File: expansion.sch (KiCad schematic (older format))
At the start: 3 parts, among them CN1 Expansion bus

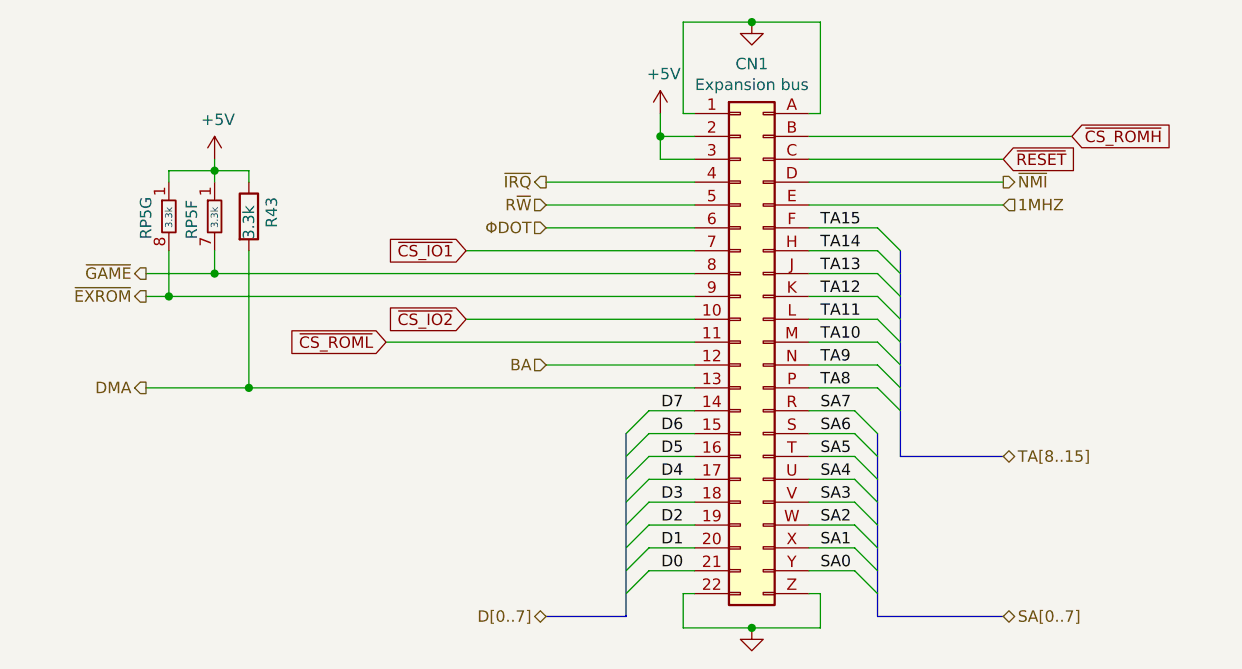
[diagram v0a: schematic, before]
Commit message: Clean up schematic
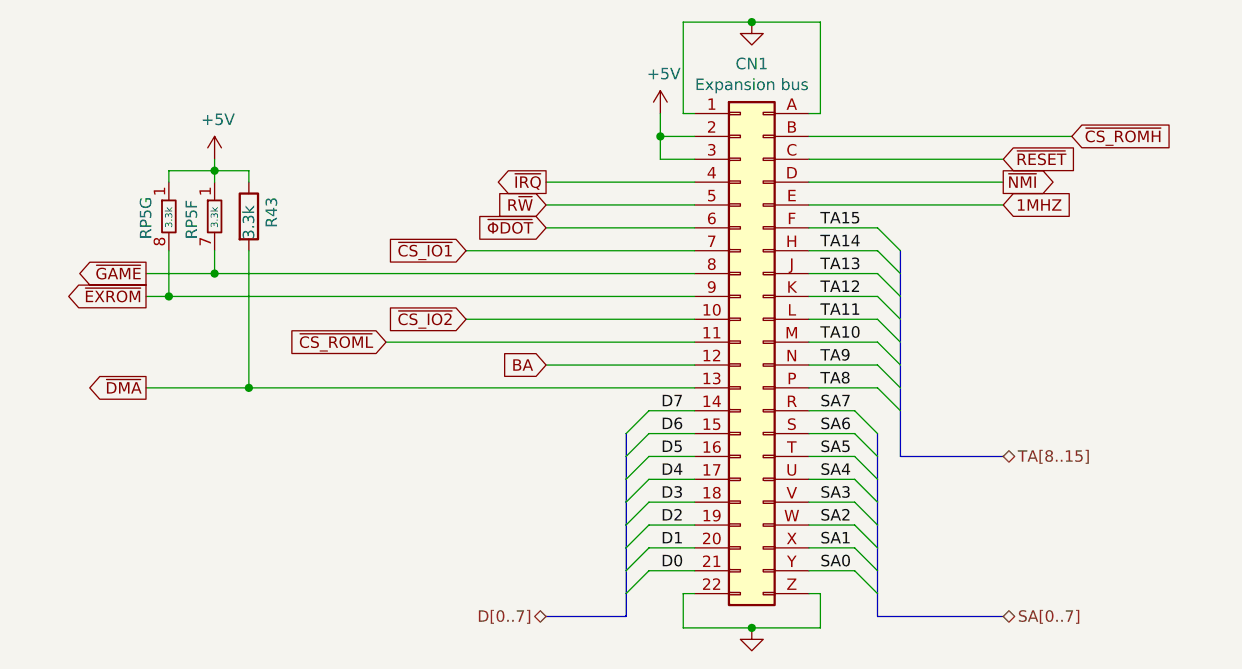
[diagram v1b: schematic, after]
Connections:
- net DMA renamed ~DMA
- net ΦDOT renamed ~ΦDOT
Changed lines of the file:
@@
 	4500 2600 4650 2600
 Connection ~ 4500 2500
-Text HLabel 4000 2700 0    50   Output ~ 0
-~IRQ
-Text HLabel 4000 2800 0    50   Input ~ 0
-R~W
-Text HLabel 4000 2900 0    50   Input ~ 0
-ΦDOT
-Text HLabel 2250 3100 0    50   Output ~ 0
-~GAME
-Text HLabel 2250 3200 0    50   Output ~ 0
-~EXROM
-Text HLabel 4000 3500 0    50   Input ~ 0
-BA
-Text HLabel 2250 3600 0    50   Output ~ 0
-DMA
 Wire Wire Line
 	4650 3700 4450 3700
@@
 Wire Wire Line
 	4000 2700 4650 2700
-Text HLabel 6000 2700 2    50   Output ~ 0
-~NMI
-Text HLabel 6000 2800 2    50   Input ~ 0
-1MHZ
 Wire Wire Line
 	5150 2800 6000 2800
@@
 Wire Bus Line
 	5550 3000 5550 3900
+Text GLabel 4000 2700 0    50   Output ~ 0
+~IRQ
+Text GLabel 4000 3500 0    50   Input ~ 0
+BA
+Text GLabel 6000 2700 2    50   Output ~ 0
+~NMI
+Text GLabel 4000 2800 0    50   Input ~ 0
+R~W
+Text GLabel 4000 2900 0    50   Input ~ 0
+~ΦDOT
+Text GLabel 6000 2800 2    50   Input ~ 0
+1MHZ
+Text GLabel 2250 3600 0    50   Output ~ 0
+~DMA
+Text GLabel 2250 3100 0    50   Output ~ 0
+~GAME
+Text GLabel 2250 3200 0    50   Output ~ 0
+~EXROM
 $EndSCHEMATC
